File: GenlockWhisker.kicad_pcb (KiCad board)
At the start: 4 copper layers, 30 x 21 mm, 30 parts, among them J1 HDBNC-J-P-XX-ST-EM1, Q1 MMBT3904, U1 LMH1980MM/NOPB

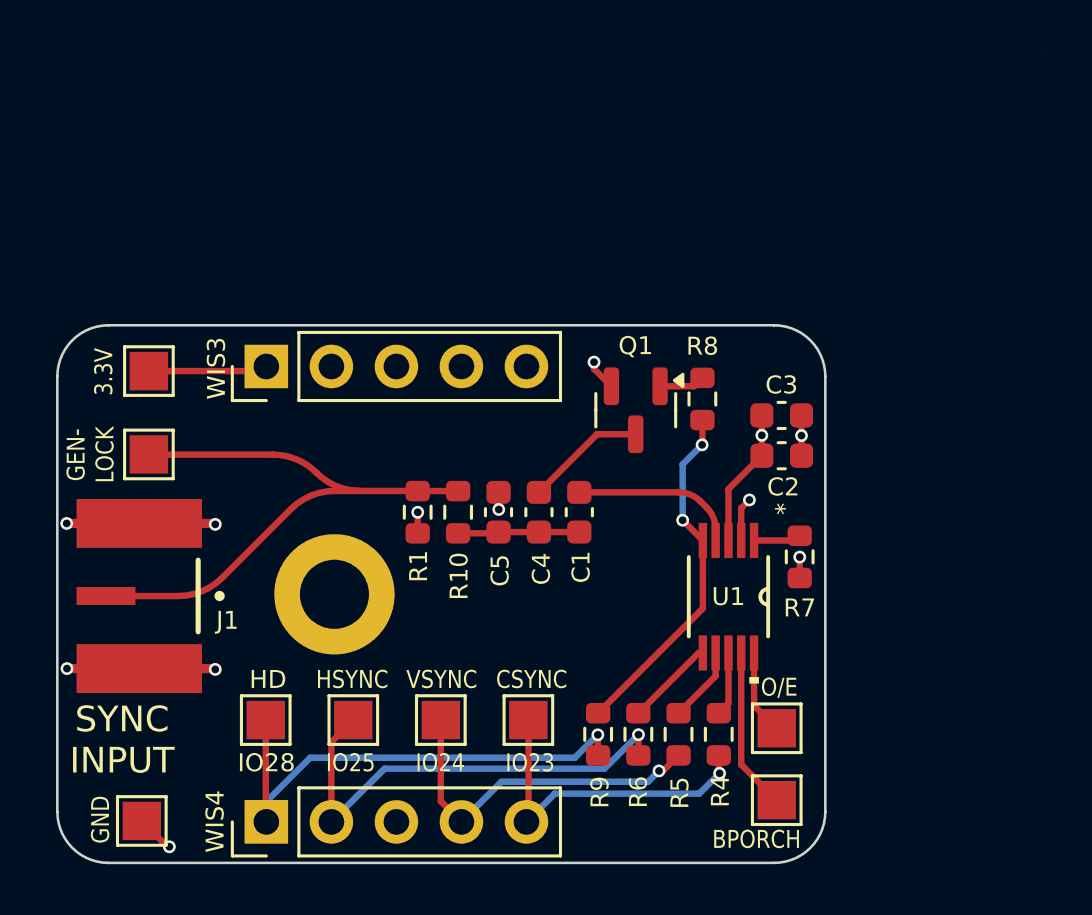
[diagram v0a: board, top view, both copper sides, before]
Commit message: New version with full size connector. major software improvements including high frequency logging and webserial UI
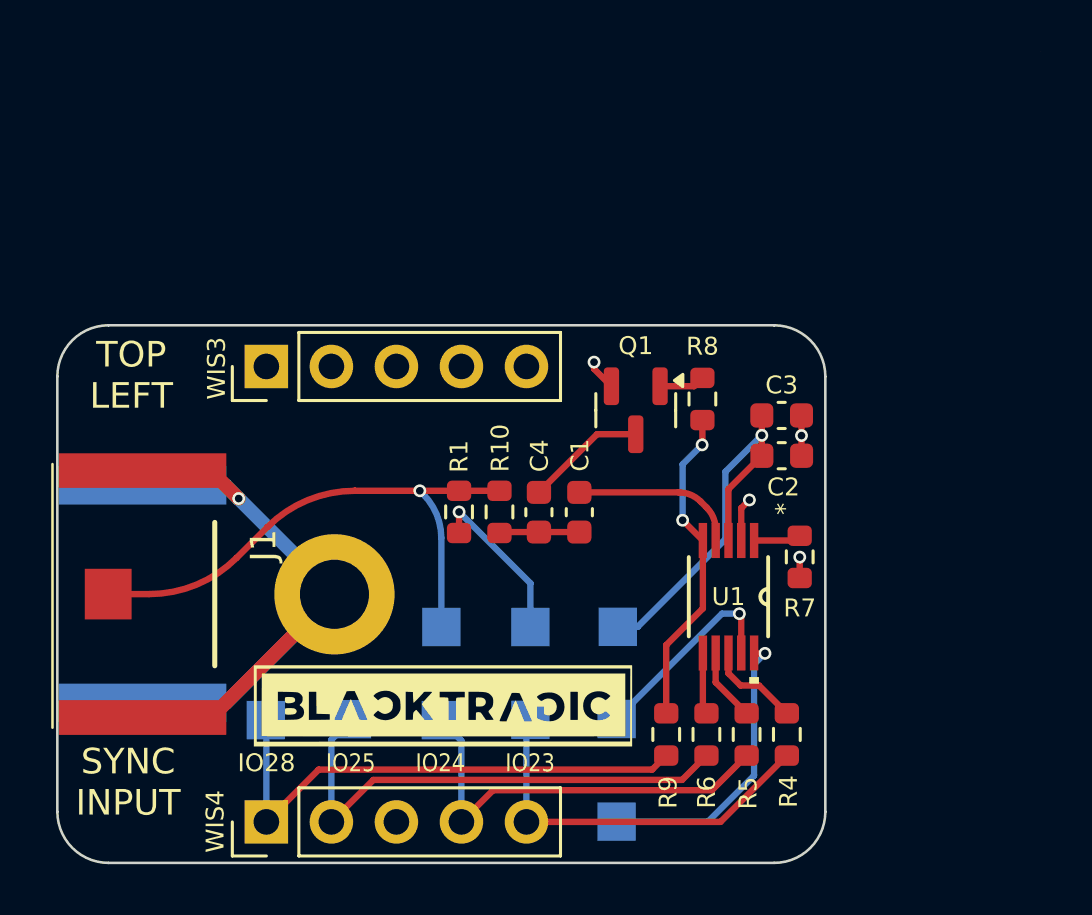
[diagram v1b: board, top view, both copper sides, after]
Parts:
- removed C5: OPT, Capacitor_SMD:C_0603_1608Metric
- G***: moved to F.Cu
- J1: value HDBNC-J-P-XX-ST-EM1 -> BNC7T-J-P-XX-ST-EM1; footprint HDBNC-J-P-GN-ST-EM1:SAMTEC_HDBNC-J-P-XX-ST-EM1 -> BNC7T_J_P_GN_ST_EM1D-3:SAMTEC_BNC7T-J-P-XX-ST-EM1D
- TP1, TP10, TP2, TP3, TP4, TP5, TP7, TP8, TP9: moved to B.Cu
- moved TP10 20.9 mm to (221.9, 111.8), turned to 180 degrees
- moved TP2 17.0 mm to (218.5, 111.8), turned to 180 degrees
- moved TP5 13.3 mm to (215.0, 111.8), turned to 180 degrees
- moved G*** 11.2 mm to (220.2, 109.9), turned to 0 degrees
- moved G*** 8.06 mm to (215.1, 114.9), turned to 90 degrees
- moved TP9 7.24 mm to (221.8, 119.4), turned to 180 degrees
- moved TP8 7.01 mm to (221.8, 115.4), turned to 180 degrees
- moved R4 2.66 mm to (228.5, 116.0)
- moved R5 2.66 mm to (226.9, 116.0)
- moved R9 2.66 mm to (223.8, 116.0)
- moved R6 2.66 mm to (225.4, 116.0)
- moved J1 2.10 mm to (199.8, 110.5), turned to -90 degrees
- moved R1 1.62 mm to (215.7, 107.3)
- moved R10 1.62 mm to (217.3, 107.3)
- moved TP4 0.08 mm to (218.5, 115.4), turned to 180 degrees
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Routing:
- net GND: track 21.9 -> 45.9 mm, vias 11 -> 6
- net Net-(U1-OE_OUT): track 3.31 -> 11.5 mm, vias 0 -> 1
- net /PI_A_3v3: track 10.3 -> 16.0 mm
- net /DI_24: track 13.9 -> 16.5 mm, vias 1 -> 0
- net /DI_23: track 13.1 -> 15.4 mm, vias 1 -> 0
- net Net-(J1-Pad1): track 24.2 -> 22.1 mm, vias 0 -> 1
- net Net-(U1-BP_OUT): track 6.32 -> 8.07 mm, vias 0 -> 1
- net Net-(C1-Pad1): track 4.76 -> 3.14 mm
- net /DI_25: track 18.6 -> 20.1 mm, vias 1 -> 0
- net Net-(U1-CS_OUT): track 2.51 -> 3.72 mm
- net Net-(U1-~HD): track 13.8 -> 12.7 mm
- net Net-(U1-HS_OUT): track 3.49 -> 2.41 mm
- net /AN_ADC2: track 19.6 -> 20.7 mm, vias 1 -> 0
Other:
- board text added: "23"
- board text added: "24"
- board text added: "25"
- board text added: "ADC_2"
- board text added: "EXPANSION PORT BOTTOM SIDE TOWARDS CENTER"
- board text added: "G"
- board text added: "G-LOCK"
- board text added: "HAPPY HOLIDAYS FROM FUSE CATS"
- board text added: "RIGHT EDGE"
- board text added: "TOP LEFT"
- board text added: "V2.1 11/25/25 M.KOHLER"
- board text removed: "(VIDEO DEVICES IN YOUR AREA)"
- board text removed: "ADC#2"
- board text removed: "GEN- LOCK"
- board text removed: "IO#23"
- board text removed: "IO#24"
- board text removed: "IO#25"
- board text removed: "V2.0 08/28/25 M.KOHLER"
